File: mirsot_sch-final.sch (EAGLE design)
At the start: 43 parts, among them IC1 7805T, IC2 MEGA16-P, M1 WIRELESS-NRF24L01

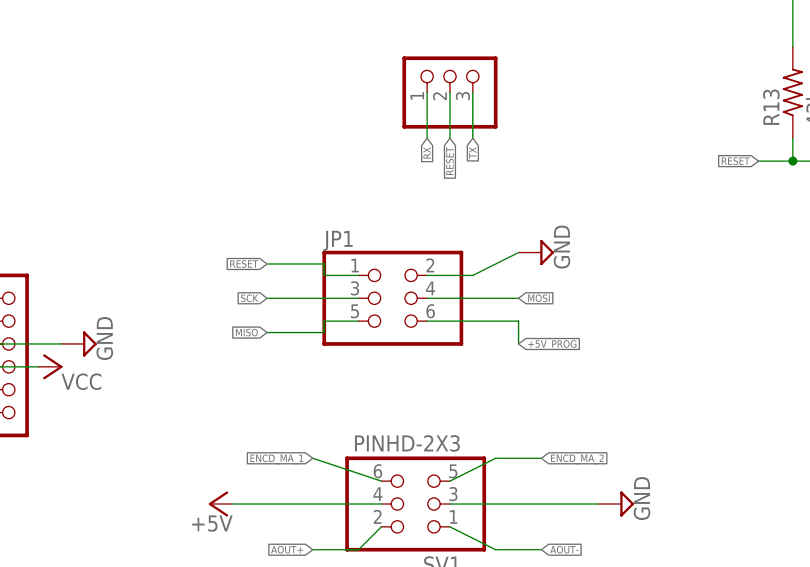
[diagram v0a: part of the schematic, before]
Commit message: shifted NRF module
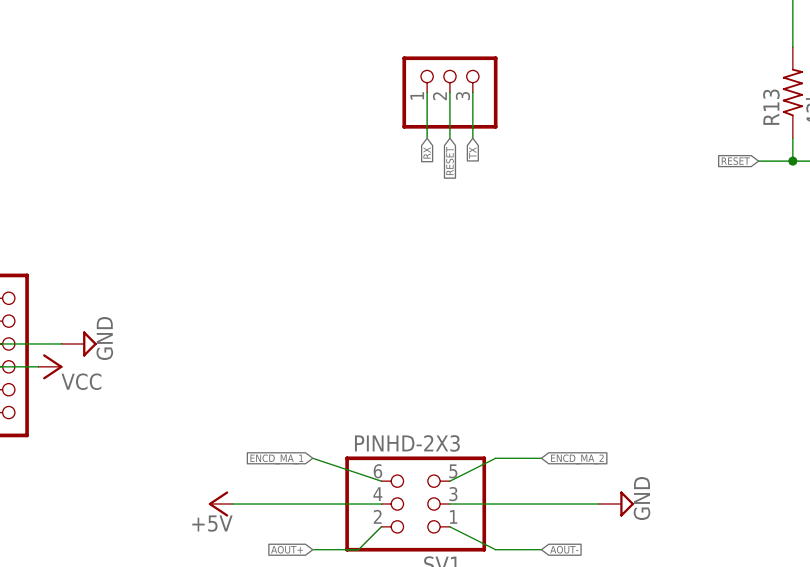
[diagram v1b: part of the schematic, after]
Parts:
- removed JP1: (no value), pinhead:PINHD-2X3/90
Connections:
- net +5V_PROG: no longer JP1.6
- net GND: no longer JP1.2
- net MISO: no longer JP1.5
- net MOSI: no longer JP1.4
- net RESET: no longer JP1.1
- net SCK: no longer JP1.3
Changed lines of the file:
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@@
 <part name="P+6" library="supply1" library_urn="urn:adsk.eagle:library:371" deviceset="+5V" device=""/>
 <part name="+3V1" library="supply1" library_urn="urn:adsk.eagle:library:371" deviceset="+3V3" device=""/>
-<part name="JP1" library="pinhead" library_urn="urn:adsk.eagle:library:325" deviceset="PINHD-2X3" device="/90" package3d_urn="urn:adsk.eagle:package:22464/2"/>
 <part name="SV1" library="Connector" library_urn="urn:adsk.eagle:library:16378166" deviceset="PINHD-2X3" device="" package3d_urn="urn:adsk.eagle:package:22462/2"/>
 <part name="P+12" library="supply1" library_urn="urn:adsk.eagle:library:371" deviceset="+5V" device=""/>
@@
 <part name="R3" library="rcl" library_urn="urn:adsk.eagle:library:334" deviceset="R-US_" device="M1206" package3d_urn="urn:adsk.eagle:package:23566/2" value="43k"/>
 <part name="P+9" library="supply1" library_urn="urn:adsk.eagle:library:371" deviceset="+5V" device=""/>
-<part name="SUPPLY10" library="supply2" library_urn="urn:adsk.eagle:library:372" deviceset="GND" device=""/>
 </parts>
 <sheets>
@@
 <attribute name="VALUE" x="53.34" y="108.204" size="1.778" layer="96" rot="R90"/>
 </instance>
-<instance part="JP1" gate="A" x="91.44" y="20.32" smashed="yes">
-<attribute name="NAME" x="85.09" y="26.035" size="1.778" layer="95"/>
-<attribute name="VALUE" x="85.09" y="12.7" size="1.778" layer="96"/>
-</instance>
 <instance part="SV1" gate="A" x="96.52" y="-2.54" smashed="yes" rot="R180">
 <attribute name="VALUE" x="100.33" y="5.08" size="1.778" layer="96" rot="R180"/>
@@
 <instance part="P+9" gate="1" x="25.4" y="-7.62" smashed="yes" rot="R180">
 <attribute name="VALUE" x="26.67" y="-5.08" size="1.778" layer="96" rot="R270"/>
-</instance>
-<instance part="SUPPLY10" gate="GND" x="109.22" y="25.4" smashed="yes" rot="R90">
-<attribute name="VALUE" x="112.395" y="23.495" size="1.778" layer="96" rot="R90"/>
 </instance>
 </instances>
@@
 <junction x="160.02" y="25.4"/>
 </segment>
-<segment>
-<pinref part="JP1" gate="A" pin="2"/>
-<wire x1="96.52" y1="22.86" x2="101.6" y2="22.86" width="0.1524" layer="91"/>
-<wire x1="101.6" y1="22.86" x2="106.68" y2="25.4" width="0.1524" layer="91"/>
-<pinref part="SUPPLY10" gate="GND" pin="GND"/>
-</segment>
 </net>
 <net name="BIN2" class="2">
@@
 <net name="MOSI" class="2">
 <segment>
-<pinref part="JP1" gate="A" pin="4"/>
-<wire x1="96.52" y1="20.32" x2="106.68" y2="20.32" width="0.1524" layer="91"/>
-<label x="106.68" y="20.32" size="0.8128" layer="95" xref="yes"/>
-</segment>
-<segment>
 <wire x1="218.44" y1="7.62" x2="220.98" y2="7.62" width="0.1524" layer="91"/>
 <label x="220.98" y="7.62" size="0.8128" layer="95" xref="yes"/>
@@
 <label x="266.7" y="119.38" size="0.8128" layer="95" rot="R180" xref="yes"/>
 </segment>
-<segment>
-<pinref part="JP1" gate="A" pin="5"/>
-<wire x1="88.9" y1="17.78" x2="85.09" y2="17.78" width="0.1524" layer="91"/>
-<wire x1="85.09" y1="17.78" x2="85.09" y2="16.51" width="0.1524" layer="91"/>
-<wire x1="85.09" y1="16.51" x2="78.74" y2="16.51" width="0.1524" layer="91"/>
-<label x="78.74" y="16.51" size="0.8128" layer="95" rot="R180" xref="yes"/>
-</segment>
 </net>
 <net name="SCK" class="2">
-<segment>
-<pinref part="JP1" gate="A" pin="3"/>
-<wire x1="88.9" y1="20.32" x2="78.74" y2="20.32" width="0.1524" layer="91"/>
-<label x="78.74" y="20.32" size="0.8128" layer="95" rot="R180" xref="yes"/>
-</segment>
 <segment>
 <wire x1="218.44" y1="12.7" x2="220.98" y2="12.7" width="0.1524" layer="91"/>
@@
 <label x="38.1" y="-17.78" size="0.8128" layer="95" rot="R180" xref="yes"/>
 </segment>
-<segment>
-<pinref part="JP1" gate="A" pin="6"/>
-<wire x1="96.52" y1="17.78" x2="106.68" y2="17.78" width="0.1524" layer="91"/>
-<wire x1="106.68" y1="17.78" x2="106.68" y2="15.24" width="0.1524" layer="91"/>
-<label x="106.68" y="15.24" size="0.8128" layer="95" xref="yes"/>
-</segment>
 </net>
 <net name="+5V_SUPPLY" class="1">
@@
 <wire x1="149.86" y1="35.56" x2="177.8" y2="35.56" width="0.1524" layer="91"/>
 </segment>
-<segment>
-<pinref part="JP1" gate="A" pin="1"/>
-<wire x1="88.9" y1="22.86" x2="85.09" y2="22.86" width="0.1524" layer="91"/>
-<wire x1="85.09" y1="22.86" x2="85.09" y2="24.13" width="0.1524" layer="91"/>
-<wire x1="85.09" y1="24.13" x2="78.74" y2="24.13" width="0.1524" layer="91"/>
-<label x="78.74" y="24.13" size="0.8128" layer="95" rot="R180" xref="yes"/>
-</segment>
-</net>
+</net>

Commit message: finalized pcb
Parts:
- removed CN2: (no value), adafruit:JST_2PIN-THM
- added J1: XT60-M, XT60-M:XT60-M
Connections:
- net GND: now also J1.NEG; no longer CN2.1
- net VCC: now also J1.POS; no longer CN2.2
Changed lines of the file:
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@@
 <class number="1" name="power" width="1.27" drill="0.75">
 </class>
-<class number="2" name="signal" width="0.508" drill="0.00635">
+<class number="2" name="signal" width="0.381" drill="0.00508125">
 </class>
 </classes>
@@
 <part name="JP2" library="pinhead" library_urn="urn:adsk.eagle:library:325" deviceset="PINHD-1X3" device="/90" package3d_urn="urn:adsk.eagle:package:22459/2"/>
 <part name="P+1" library="supply1" library_urn="urn:adsk.eagle:library:371" deviceset="+5V" device=""/>
-<part name="CN2" library="adafruit" deviceset="JST_2PIN" device="-THM"/>
 <part name="U$2" library="LM1117-3.3" deviceset="LM1117-3.3" device=""/>
 <part name="P+5" library="supply1" library_urn="urn:adsk.eagle:library:371" deviceset="+5V" device=""/>
@@
 <part name="R3" library="rcl" library_urn="urn:adsk.eagle:library:334" deviceset="R-US_" device="M1206" package3d_urn="urn:adsk.eagle:package:23566/2" value="43k"/>
 <part name="P+9" library="supply1" library_urn="urn:adsk.eagle:library:371" deviceset="+5V" device=""/>
+<part name="J1" library="XT60-M" deviceset="XT60-M" device=""/>
 </parts>
 <sheets>
@@
 <attribute name="VALUE" x="54.61" y="-16.51" size="1.778" layer="96" rot="R90"/>
 </instance>
-<instance part="CN2" gate="G$1" x="68.58" y="129.54" smashed="yes" rot="R180">
-<attribute name="NAME" x="74.93" y="123.825" size="1.778" layer="95" rot="R180"/>
-<attribute name="VALUE" x="74.93" y="134.62" size="1.778" layer="96" rot="R180"/>
-</instance>
 <instance part="U$2" gate="G$1" x="154.94" y="96.52" smashed="yes">
 <attribute name="NAME" x="147.666159375" y="100.56385" size="2.085509375" layer="95" ratio="10" rot="SR0"/>
@@
 <instance part="P+9" gate="1" x="25.4" y="-7.62" smashed="yes" rot="R180">
 <attribute name="VALUE" x="26.67" y="-5.08" size="1.778" layer="96" rot="R270"/>
+</instance>
+<instance part="J1" gate="G$1" x="68.58" y="127" smashed="yes">
+<attribute name="NAME" x="68.58" y="133.35" size="1.778" layer="95"/>
+<attribute name="VALUE" x="68.58" y="121.92" size="1.778" layer="96"/>
 </instance>
 </instances>
@@
 </segment>
 <segment>
-<pinref part="CN2" gate="G$1" pin="1"/>
 <pinref part="SUPPLY1" gate="GND" pin="GND"/>
-<wire x1="71.12" y1="127" x2="71.12" y2="113.03" width="0.1524" layer="91"/>
-<wire x1="71.12" y1="113.03" x2="80.01" y2="113.03" width="0.1524" layer="91"/>
+<wire x1="63.5" y1="113.03" x2="80.01" y2="113.03" width="0.1524" layer="91"/>
 <pinref part="R7" gate="G$1" pin="1"/>
 <wire x1="80.01" y1="113.03" x2="88.9" y2="113.03" width="0.1524" layer="91"/>
@@
 <wire x1="80.01" y1="125.73" x2="80.01" y2="113.03" width="0.1524" layer="91"/>
 <junction x="80.01" y="113.03"/>
+<wire x1="63.5" y1="127" x2="63.5" y2="113.03" width="0.1524" layer="91"/>
+<pinref part="J1" gate="G$1" pin="NEG"/>
 </segment>
 <segment>
@@
 <wire x1="96.52" y1="139.7" x2="96.52" y2="142.24" width="0.1524" layer="91"/>
 <wire x1="96.52" y1="142.24" x2="87.63" y2="142.24" width="0.1524" layer="91"/>
-<wire x1="71.12" y1="142.24" x2="80.01" y2="142.24" width="0.1524" layer="91"/>
+<wire x1="63.5" y1="142.24" x2="80.01" y2="142.24" width="0.1524" layer="91"/>
 <junction x="80.01" y="142.24"/>
 <pinref part="P+2" gate="VCC" pin="VCC"/>
-<pinref part="CN2" gate="G$1" pin="2"/>
-<wire x1="71.12" y1="129.54" x2="71.12" y2="142.24" width="0.1524" layer="91"/>
-</segment>
-<segment>
+<wire x1="63.5" y1="129.54" x2="63.5" y2="142.24" width="0.1524" layer="91"/>
+<pinref part="J1" gate="G$1" pin="POS"/>
+</segment>
+<segment>

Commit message: changed battery connecter orientation
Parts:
- removed J1: XT60-M, XT60-M:XT60-M
- added U$1: T_PLUG_CONNECTOR_H, con-T-plug:T_PLUG_CONNECTOR_H
- IC1: value 7805T -> 7805DT; device linear:7805T -> linear:7805DT
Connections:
- net GND: now also U$1.P-2; no longer J1.NEG
- net VCC: now also U$1.P-1; no longer J1.POS
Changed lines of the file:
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@@
 <part name="C4" library="rcl" library_urn="urn:adsk.eagle:library:334" deviceset="C-US" device="C0603K" package3d_urn="urn:adsk.eagle:package:23680/2" value="100n"/>
 <part name="C5" library="rcl" library_urn="urn:adsk.eagle:library:334" deviceset="C-US" device="C0603K" package3d_urn="urn:adsk.eagle:package:23680/2" value="100n"/>
-<part name="IC1" library="linear" library_urn="urn:adsk.eagle:library:262" deviceset="78*" device="T" package3d_urn="urn:adsk.eagle:package:16414/1" technology="05" value="7805T"/>
+<part name="IC1" library="linear" library_urn="urn:adsk.eagle:library:262" deviceset="78*" device="DT" package3d_urn="urn:adsk.eagle:package:16415/2" technology="05" value="7805DT"/>
 <part name="R4" library="rcl" library_urn="urn:adsk.eagle:library:334" deviceset="R-US_" device="M1206" package3d_urn="urn:adsk.eagle:package:23566/2" value="330"/>
 <part name="5VLD" library="led" library_urn="urn:adsk.eagle:library:259" deviceset="LED" device="SML1206" package3d_urn="urn:adsk.eagle:package:15829/1" value="RED"/>
@@
 <part name="R3" library="rcl" library_urn="urn:adsk.eagle:library:334" deviceset="R-US_" device="M1206" package3d_urn="urn:adsk.eagle:package:23566/2" value="43k"/>
 <part name="P+9" library="supply1" library_urn="urn:adsk.eagle:library:371" deviceset="+5V" device=""/>
-<part name="J1" library="XT60-M" deviceset="XT60-M" device=""/>
+<part name="U$1" library="con-T-plug" deviceset="T_PLUG_CONNECTOR_H" device=""/>
 </parts>
 <sheets>
@@
 <attribute name="VALUE" x="26.67" y="-5.08" size="1.778" layer="96" rot="R270"/>
 </instance>
-<instance part="J1" gate="G$1" x="68.58" y="127" smashed="yes">
-<attribute name="NAME" x="68.58" y="133.35" size="1.778" layer="95"/>
-<attribute name="VALUE" x="68.58" y="121.92" size="1.778" layer="96"/>
-</instance>
+<instance part="U$1" gate="G$1" x="66.04" y="134.62" smashed="yes" rot="R270"/>
 </instances>
 <busses>
@@
 <junction x="80.01" y="113.03"/>
 <wire x1="63.5" y1="127" x2="63.5" y2="113.03" width="0.1524" layer="91"/>
-<pinref part="J1" gate="G$1" pin="NEG"/>
+<pinref part="U$1" gate="G$1" pin="P-2"/>
 </segment>
 <segment>
@@
 <junction x="80.01" y="142.24"/>
 <pinref part="P+2" gate="VCC" pin="VCC"/>
-<wire x1="63.5" y1="129.54" x2="63.5" y2="142.24" width="0.1524" layer="91"/>
-<pinref part="J1" gate="G$1" pin="POS"/>
-</segment>
-<segment>
+<wire x1="63.5" y1="132.08" x2="63.5" y2="142.24" width="0.1524" layer="91"/>
+<pinref part="U$1" gate="G$1" pin="P-1"/>
+</segment>
+<segment>

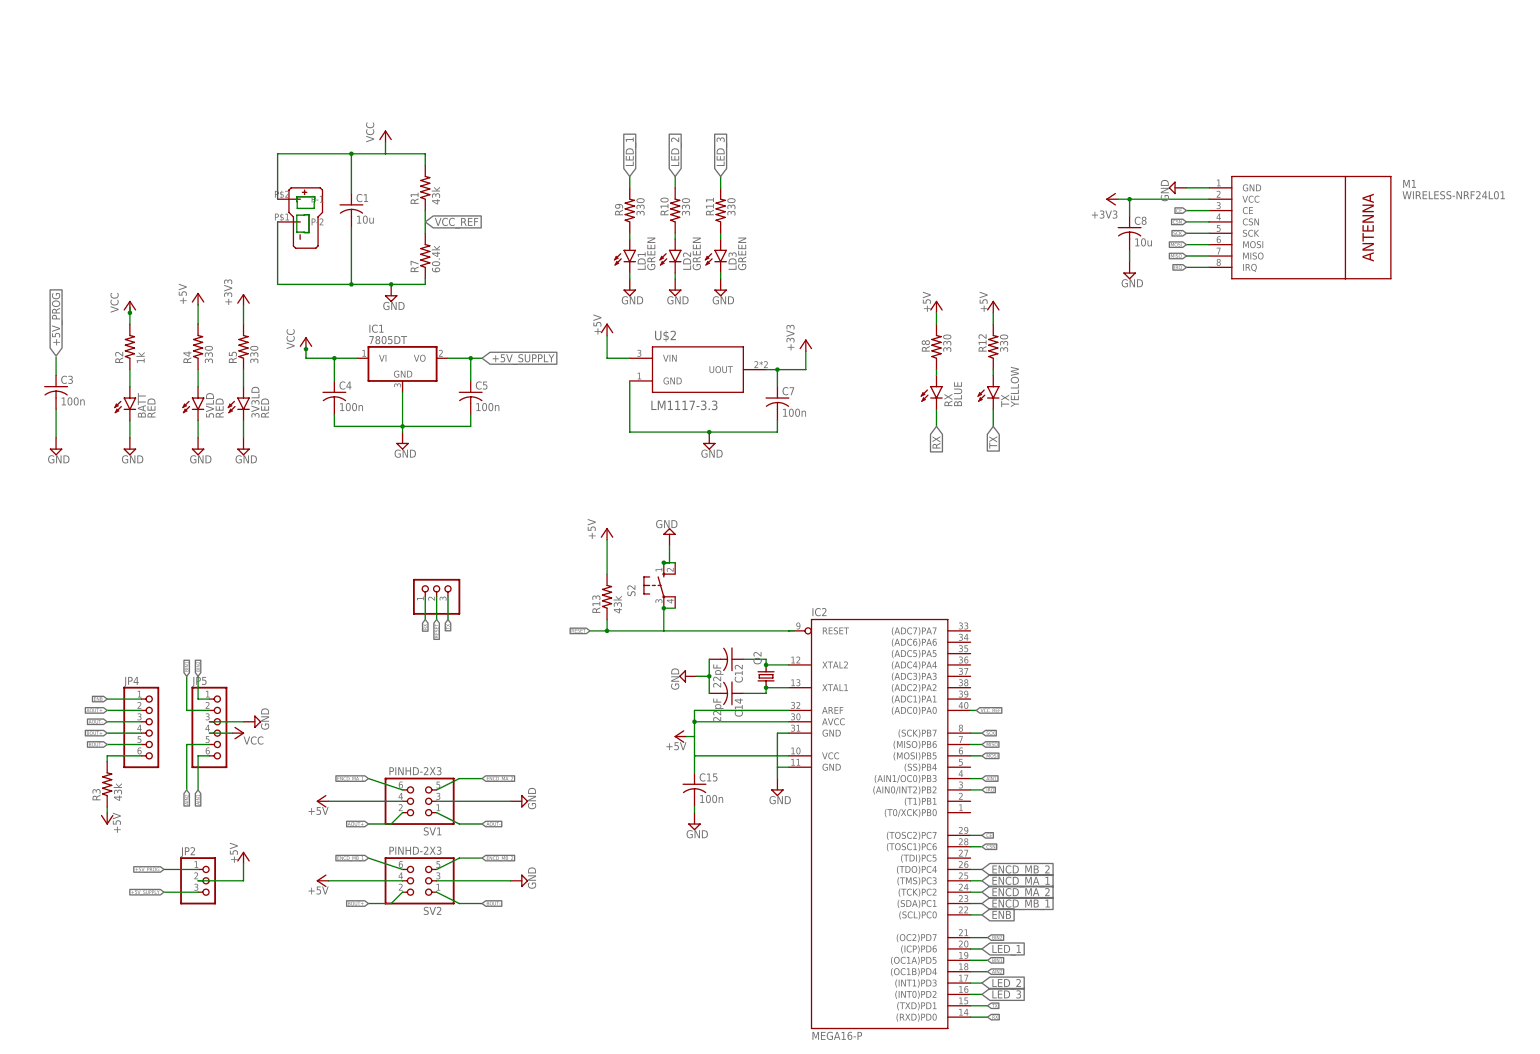
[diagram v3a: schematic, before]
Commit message: changed mcu to esp32
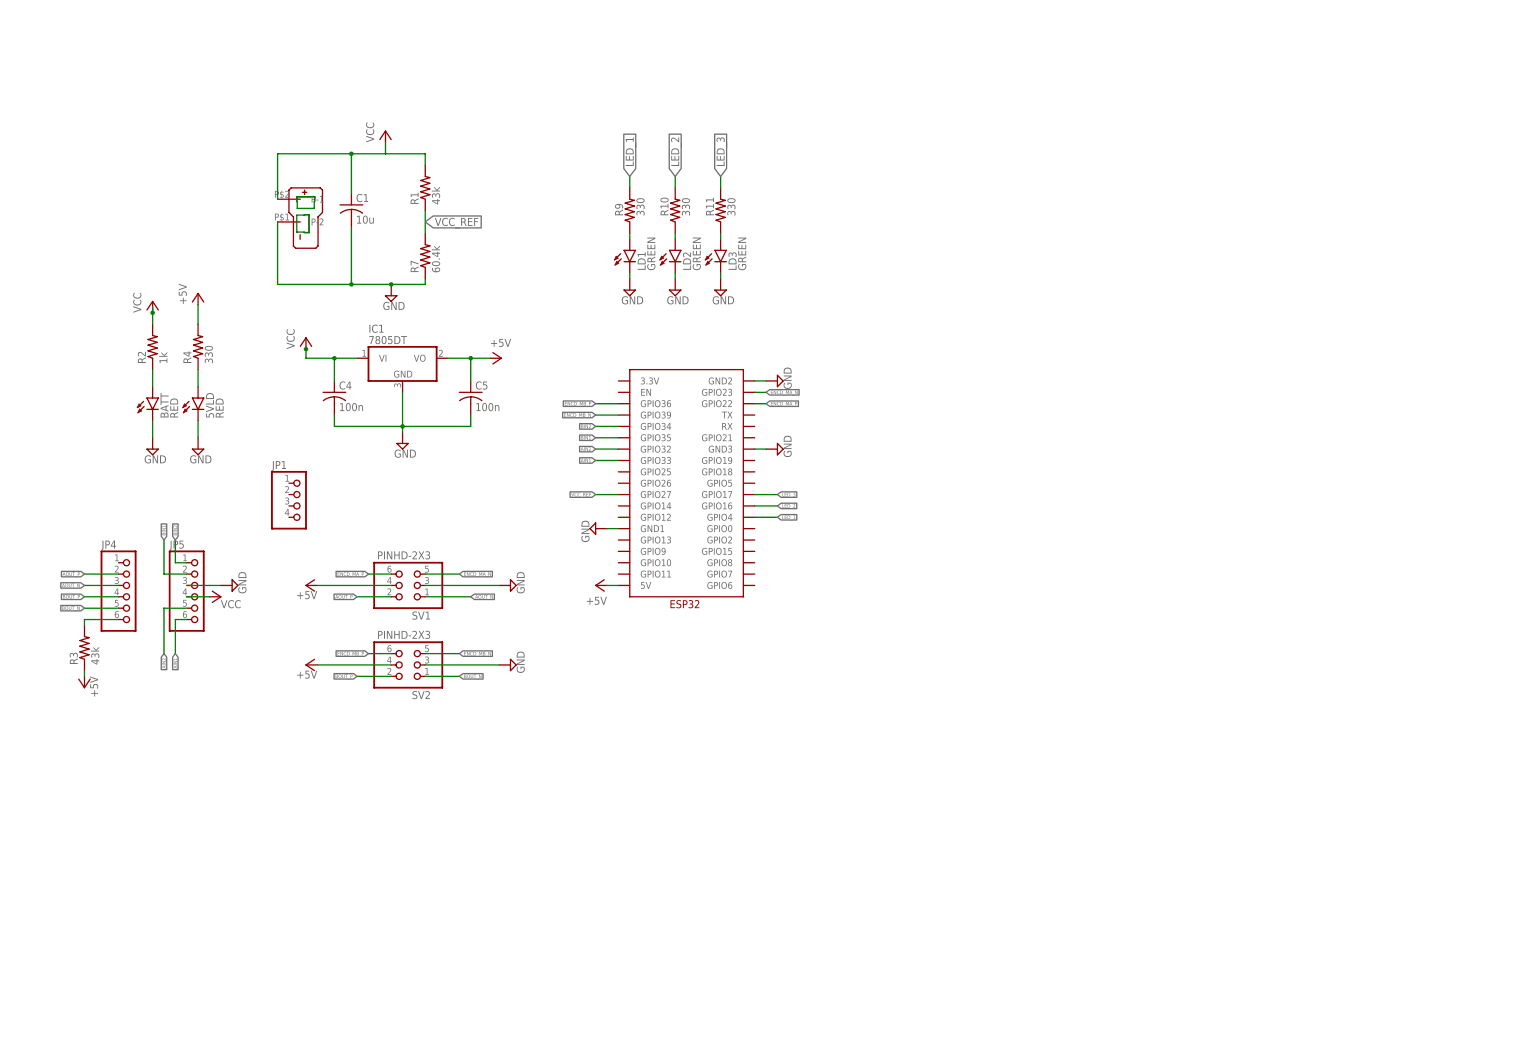
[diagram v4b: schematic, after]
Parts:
- removed 3V3LD: RED, led:LEDSML1206
- removed C12, C14: 22pF, rcl:C-US025-025X050
- removed C15: 100n, rcl:C-USC0603K
- removed C3: 100n, rcl:C-USC1206K
- removed C7: 100n, rcl:C-USC0603
- removed C8: 10u, rcl:C-USC1206K
- removed IC2: MEGA16-P, atmel:MEGA16-P
- removed JP2, JP3: (no value), pinhead:PINHD-1X3/90
- removed M1: WIRELESS-NRF24L01, diy-modules:WIRELESS-NRF24L01
- removed Q2: (no value), crystal:CRYSTALHC49S
- removed R12, R5, R8: 330, rcl:R-US_M1206
- removed R13: 43k, rcl:R-US_M1206
- removed RX: BLUE, led:LEDSML1206
- removed S2: (no value), switch-omron:10-XX
- removed TX: YELLOW, led:LEDSML1206
- added JP1: (no value), pinhead:PINHD-1X4
- U$2: value LM1117-3.3 -> ESP32; device LM1117-3.3:LM1117-3.3 -> ESP32:ESP32
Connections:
- net AOUT+ renamed AOUT_P
- net AOUT- renamed AOUT_N
- net BOUT+ renamed BOUT_P
- net BOUT- renamed BOUT_N
- removed net +3V3: C7.1, C8.1, M1.VCC, R5.2, U$2.UOUT
- removed net +5V_PROG: C3.1, JP2.1
- removed net +5V_SUPPLY: C5.1, IC1.VO, JP2.3
- removed net CE: IC2.(TOSC2)PC7, M1.CE
- removed net CSN: IC2.(TOSC1)PC6, M1.CSN
- removed net ENB: IC2.(SCL)PC0, JP4.1
- removed net ENCD_MA_1: IC2.(TMS)PC3, SV1.6
- removed net ENCD_MA_2: IC2.(TCK)PC2, SV1.5
- removed net ENCD_MB_1: IC2.(SDA)PC1, SV2.6
- removed net ENCD_MB_2: IC2.(TDO)PC4, SV2.5
- removed net IRQ: IC2.(AIN0/INT2)PB2, M1.IRQ
- removed net MISO: IC2.(MISO)PB6, M1.MISO
- removed net MOSI: IC2.(MOSI)PB5, M1.MOSI
- removed net N$10: R8.1, RX.A
- removed net N$11: R12.1, TX.A
- removed net N$12: C12.1, IC2.XTAL2, Q2.2
- removed net N$13: C14.1, IC2.XTAL1, Q2.1
- removed net N$6: 3V3LD.A, R5.1
- removed net RESET: IC2.RESET, JP3.2, R13.1, S2.P, S2.P1
- removed net RX: IC2.(RXD)PD0, JP3.1, RX.C
- removed net SCK: IC2.(SCK)PB7, M1.SCK
- removed net TX: IC2.(TXD)PD1, JP3.3, TX.C
- new net ENCD_MA_N: SV1.5, U$2.GPIO23
- new net ENCD_MA_P: SV1.6, U$2.GPIO22
- new net ENCD_MB_N: SV2.5, U$2.GPIO39
- new net ENCD_MB_P: SV2.6, U$2.GPIO36
- net +5V: now also C5.1, IC1.VO, U$2.5V; no longer C15.1, IC2.AREF, IC2.AVCC, IC2.VCC, JP2.2, R12.2, R13.2, R8.2, U$2.VIN
- net AIN1: now also U$2.GPIO33; no longer IC2.(AIN1/OC0)PB3
- net AIN2: now also U$2.GPIO32; no longer IC2.(OC1B)PD4
- net BIN1: now also U$2.GPIO35; no longer IC2.(OC1A)PD5
- net BIN2: now also U$2.GPIO34; no longer IC2.(OC2)PD7
- net GND: now also U$2.GND1, U$2.GND2, U$2.GND3; no longer 3V3LD.C, C12.2, C14.2, C15.2, C3.2, C7.2, C8.2, IC2.GND, IC2.GND@1, M1.GND, S2.S, S2.S1, U$2.GND
- net LED_1: now also U$2.GPIO4; no longer IC2.(ICP)PD6
- net LED_2: now also U$2.GPIO16; no longer IC2.(INT1)PD3
- net LED_3: now also U$2.GPIO17; no longer IC2.(INT0)PD2
- net VCC_REF: now also U$2.GPIO27; no longer IC2.(ADC0)PA0
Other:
- moved on the sheet: BATT, JP4, JP5, R2, R3, SV1, SV2
